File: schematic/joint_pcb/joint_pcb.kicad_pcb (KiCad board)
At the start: 2 copper layers, 0 parts

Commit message: joint pcb power section
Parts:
- added C1: 100u, Capacitor_THT:CP_Radial_D5.0mm_P2.00mm, F.Cu at (64.5, 95.0)
- added C10: 56n, Capacitor_THT:C_Disc_D5.0mm_W2.5mm_P5.00mm, F.Cu at (98.6, 128.9)
- added C11: 5.6n, Capacitor_THT:C_Disc_D5.0mm_W2.5mm_P5.00mm, F.Cu at (106.8, 120.8)
- added C12: 56n, Capacitor_THT:C_Disc_D5.0mm_W2.5mm_P5.00mm, F.Cu at (106.8, 124.9)
- added C13: 100u, Capacitor_THT:CP_Radial_D5.0mm_P2.00mm, F.Cu at (88.9, 94.2)
- added C14: 100nF, Capacitor_THT:C_Disc_D5.0mm_W2.5mm_P5.00mm, F.Cu at (93.8, 137.0)
- added C15: ECE-A1HN101U, Capacitor_THT:CP_Radial_D10.0mm_P5.00mm, F.Cu at (51.8, 73.2)
- added C16: C324C106K3R5TA, Capacitor_THT:C_Disc_D3.8mm_W2.6mm_P2.50mm, F.Cu at (55.9, 60.5)
- added C17: K104Z15Y5VE5TL2, Capacitor_THT:C_Disc_D3.8mm_W2.6mm_P2.50mm, F.Cu at (49.8, 60.5)
- added C18: ECA-1EM100B, Capacitor_THT:CP_Radial_Tantal_D5.0mm_P5.00mm, F.Cu at (81.5, 84.3)
- added C19: ECA-1EM100B, Capacitor_THT:CP_Radial_Tantal_D5.0mm_P5.00mm, F.Cu at (76.5, 52.6)
- added C2: 10u, Capacitor_THT:CP_Radial_D5.0mm_P2.00mm, F.Cu at (79.5, 95.2)
- added C20: EEU-FC1H102L, Capacitor_THT:CP_Radial_D12.5mm_P5.00mm, F.Cu at (111.0, 47.0)
- added C21: C324C106K3R5TA, Capacitor_THT:C_Disc_D3.8mm_W2.6mm_P2.50mm, F.Cu at (136.1, 57.2)
- added C22: K104Z15Y5VE5TL2, Capacitor_THT:C_Disc_D3.8mm_W2.6mm_P2.50mm, F.Cu at (141.2, 57.2)
- added C3: 10u, Capacitor_THT:CP_Radial_D5.0mm_P2.00mm, F.Cu at (72.4, 94.0)
- added C4: 4.7n, Capacitor_THT:C_Disc_D5.0mm_W2.5mm_P5.00mm, F.Cu at (128.3, 126.0)
- added C5: 47n, Capacitor_THT:C_Disc_D5.0mm_W2.5mm_P5.00mm, F.Cu at (98.6, 133.0)
- added C6: 100nF, Capacitor_THT:C_Disc_D5.0mm_W2.5mm_P5.00mm, F.Cu at (98.6, 120.8)
- added C7: 4.7n, Capacitor_THT:C_Disc_D5.0mm_W2.5mm_P5.00mm, F.Cu at (98.6, 124.9)
- added C8: 5.6n, Capacitor_THT:C_Disc_D5.0mm_W2.5mm_P5.00mm, F.Cu at (112.0, 116.8)
- added C9: 100nF, Capacitor_THT:C_Disc_D5.0mm_W2.5mm_P5.00mm, F.Cu at (106.8, 128.9)
- added D1: 1N4148, Diode_THT:D_DO-35_SOD27_P7.62mm_Horizontal, F.Cu at (71.1, 80.8)
- added D2: 1N4148, Diode_THT:D_DO-35_SOD27_P7.62mm_Horizontal, F.Cu at (71.1, 60.5)
- added D3: 1N4148, Diode_THT:D_DO-35_SOD27_P7.62mm_Horizontal, F.Cu at (89.4, 49.5)
- added D4: 1N4148, Diode_THT:D_DO-35_SOD27_P7.62mm_Horizontal, F.Cu at (89.7, 59.7)
- added D5: 1N4148, Diode_THT:D_DO-35_SOD27_P7.62mm_Horizontal, F.Cu at (89.7, 74.9)
- added D6: 1N4148, Diode_THT:D_DO-35_SOD27_P7.62mm_Horizontal, F.Cu at (89.7, 85.1)
- added H1: MountingHole, MountingHole:MountingHole_4.3mm_M4, F.Cu at (139.2, 136.1)
- added H2: MountingHole, MountingHole:MountingHole_4.3mm_M4, F.Cu at (138.7, 48.8)
- added H3: MountingHole, MountingHole:MountingHole_4.3mm_M4, F.Cu at (49.8, 137.2)
- added H4: MountingHole, MountingHole:MountingHole_4.3mm_M4, F.Cu at (49.8, 48.8)
- added IC1: ADA4891-2ARMZ-R7, Package_SO:SOIC-8-1EP_3.9x4.9mm_P1.27mm_EP2.41x3.3mm_ThermalVias, F.Cu at (88.0, 138.2)
- added IC2: LM361N_NOPB, Package_DIP:DIP-14_W7.62mm_Socket_LongPads, F.Cu at (60.8, 124.2)
- added J1: Screw_Terminal_01x04, TerminalBlock_Phoenix:TerminalBlock_Phoenix_PT-1,5-4-3.5-H_1x04_P3.50mm_Horizontal, F.Cu at (51.8, 91.2)
- added J2: Amp_Power, TerminalBlock_Phoenix:TerminalBlock_Phoenix_PT-1,5-2-3.5-H_1x02_P3.50mm_Horizontal, F.Cu at (129.3, 49.0)
- added J3: Audio OUTPUT, TerminalBlock_Phoenix:TerminalBlock_Phoenix_PT-1,5-2-3.5-H_1x02_P3.50mm_Horizontal, F.Cu at (138.7, 72.8)
- added Q1: IRF530A, digikey-footprints:TO-220-3, F.Cu at (111.8, 66.0)
- added Q2: IRF530A, digikey-footprints:TO-220-3, F.Cu at (125.0, 66.0)
- added Q3: IRF530A, digikey-footprints:TO-220-3, F.Cu at (111.8, 76.2)
- added Q4: IRF530A, digikey-footprints:TO-220-3, F.Cu at (125.0, 76.2)
- added R1: 10k, Resistor_THT:R_Axial_DIN0207_L6.3mm_D2.5mm_P10.16mm_Horizontal, F.Cu at (101.4, 104.6)
- added R10: 10k, Resistor_THT:R_Axial_DIN0207_L6.3mm_D2.5mm_P10.16mm_Horizontal, F.Cu at (101.4, 108.7)
- added R11: 8.2k, Resistor_THT:R_Axial_DIN0207_L6.3mm_D2.5mm_P10.16mm_Horizontal, F.Cu at (72.0, 134.5)
- added R12: 1k, Resistor_THT:R_Axial_DIN0207_L6.3mm_D2.5mm_P10.16mm_Horizontal, F.Cu at (85.3, 120.8)
- added R13: 8.2k, Resistor_THT:R_Axial_DIN0207_L6.3mm_D2.5mm_P10.16mm_Horizontal, F.Cu at (114.7, 104.6)
- added R14: 680, Resistor_THT:R_Axial_DIN0207_L6.3mm_D2.5mm_P10.16mm_Horizontal, F.Cu at (85.3, 128.9)
- added R15: 15k, Resistor_THT:R_Axial_DIN0207_L6.3mm_D2.5mm_P10.16mm_Horizontal, F.Cu at (98.6, 116.8)
- added R16: 560, Resistor_THT:R_Axial_DIN0207_L6.3mm_D2.5mm_P10.16mm_Horizontal, F.Cu at (85.3, 133.0)
- added R17: 18k, Resistor_THT:R_Axial_DIN0207_L6.3mm_D2.5mm_P10.16mm_Horizontal, F.Cu at (72.0, 138.6)
- added R18: 10k, Resistor_THT:R_Axial_DIN0207_L6.3mm_D2.5mm_P10.16mm_Horizontal, F.Cu at (85.3, 124.9)
- added R19: 10k, Resistor_THT:R_Axial_DIN0207_L6.3mm_D2.5mm_P10.16mm_Horizontal, F.Cu at (101.4, 112.7)
- added R2: 1k, Resistor_THT:R_Axial_DIN0207_L6.3mm_D2.5mm_P10.16mm_Horizontal, F.Cu at (72.0, 130.5)
- added R20: 10k, Resistor_THT:R_Axial_DIN0207_L6.3mm_D2.5mm_P10.16mm_Horizontal, F.Cu at (88.1, 104.6)
- added R21: CFR-25JB-52-470R, Resistor_THT:R_Axial_DIN0207_L6.3mm_D2.5mm_P10.16mm_Horizontal, F.Cu at (71.1, 75.7)
- added R22: CFR-25JB-52-470R, Resistor_THT:R_Axial_DIN0207_L6.3mm_D2.5mm_P10.16mm_Horizontal, F.Cu at (71.1, 65.5)
- added R23: MFP-25BRD52-1K, Resistor_THT:R_Axial_DIN0207_L6.3mm_D2.5mm_P10.16mm_Horizontal, F.Cu at (71.1, 70.6)
- added R24: CFR-25JR-52-100R, Resistor_THT:R_Axial_DIN0207_L6.3mm_D2.5mm_P10.16mm_Horizontal, F.Cu at (98.6, 54.4)
- added R25: CFR-25JR-52-100R, Resistor_THT:R_Axial_DIN0207_L6.3mm_D2.5mm_P10.16mm_Horizontal, F.Cu at (98.6, 64.5)
- added R26: CFR50SJT-52-10K, Resistor_THT:R_Axial_DIN0207_L6.3mm_D2.5mm_P10.16mm_Horizontal, F.Cu at (119.4, 59.4)
- added R27: CFR50SJT-52-10K, Resistor_THT:R_Axial_DIN0207_L6.3mm_D2.5mm_P10.16mm_Horizontal, F.Cu at (132.6, 59.4)
- added R28: CFR50SJT-52-10K, Resistor_THT:R_Axial_DIN0207_L6.3mm_D2.5mm_P10.16mm_Horizontal, F.Cu at (132.6, 82.8)
- added R29: CFR50SJT-52-10K, Resistor_THT:R_Axial_DIN0207_L6.3mm_D2.5mm_P10.16mm_Horizontal, F.Cu at (119.4, 82.8)
- added R3: 10k, Resistor_THT:R_Axial_DIN0207_L6.3mm_D2.5mm_P10.16mm_Horizontal, F.Cu at (72.0, 126.4)
- added R30: CFR-25JR-52-100R, Resistor_THT:R_Axial_DIN0207_L6.3mm_D2.5mm_P10.16mm_Horizontal, F.Cu at (88.4, 69.6)
- added R31: CFR-25JR-52-100R, Resistor_THT:R_Axial_DIN0207_L6.3mm_D2.5mm_P10.16mm_Horizontal, F.Cu at (88.4, 79.8)
- added R4: 10k, Resistor_THT:R_Axial_DIN0207_L6.3mm_D2.5mm_P10.16mm_Horizontal, F.Cu at (72.0, 122.4)
- added R5: 1.2k, Resistor_THT:R_Axial_DIN0207_L6.3mm_D2.5mm_P10.16mm_Horizontal, F.Cu at (85.3, 116.8)
- added R6: 5.6k, Resistor_THT:R_Axial_DIN0207_L6.3mm_D2.5mm_P10.16mm_Horizontal, F.Cu at (72.0, 118.3)
- added R7: 10k, Resistor_THT:R_Axial_DIN0207_L6.3mm_D2.5mm_P10.16mm_Horizontal, F.Cu at (72.0, 114.3)
- added R8: 1.2k, Resistor_THT:R_Axial_DIN0207_L6.3mm_D2.5mm_P10.16mm_Horizontal, F.Cu at (88.1, 112.7)
- added R9: 10k, Resistor_THT:R_Axial_DIN0207_L6.3mm_D2.5mm_P10.16mm_Horizontal, F.Cu at (88.1, 108.7)
- added U1: LM7805_TO220, Package_TO_SOT_THT:TO-220-3_Vertical, F.Cu at (51.8, 108.5)
- added U2: LM324, Package_DIP:DIP-14_W7.62mm_Socket_LongPads, F.Cu at (60.8, 104.7)
- added U3: HIP4082IP, Package_DIP:DIP-16_W7.62mm, F.Cu at (75.2, 60.5)
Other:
- board outline added: 100 x 100 mm

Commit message: add trace
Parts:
- moved U1 185.7 mm to (237.2, 96.3), turned to 0 degrees
- moved C1 173.7 mm to (237.2, 113.8)
- moved C2 165.3 mm to (244.4, 105.7)
- moved C3 159.2 mm to (229.1, 122.4)
- moved C13 156.0 mm to (243.9, 112.2)
- moved R2 155.4 mm to (222.2, 90.4)
- moved R4 152.7 mm to (222.2, 94.4)
- moved R6 151.5 mm to (222.2, 98.5)
- moved R9 148.6 mm to (235.5, 90.4)
- moved C10 147.8 mm to (243.6, 100.4)
- moved R17 143.8 mm to (208.9, 94.4)
- moved IC1 143.3 mm to (228.0, 107.8)
- moved C5 140.7 mm to (235.5, 100.4)
- moved R11 140.5 mm to (208.9, 102.5)
- moved R7 140.0 mm to (212.0, 114.7)
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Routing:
- net Vcc: track 0.00 -> 92.3 mm
- net +15V: track 0.00 -> 87.7 mm
- net OUT+: track 0.00 -> 83.7 mm
- net OUT-: track 0.00 -> 82.9 mm
- net Net-(D5-Pad2): track 0.00 -> 39.7 mm
- net Net-(D4-Pad2): track 0.00 -> 38.8 mm
- net Net-(D3-Pad2): track 0.00 -> 21.6 mm
- net Net-(D6-Pad2): track 0.00 -> 21.5 mm
- net Net-(C18-Pad2): track 0.00 -> 19.5 mm
- net /Power stage/AHO: track 0.00 -> 17.0 mm
- net Net-(R21-Pad1): track 0.00 -> 14.8 mm
- net /Power stage/ALO: track 0.00 -> 14.8 mm
- net Net-(C19-Pad1): track 0.00 -> 14.0 mm
- net /Power stage/BLO: track 0.00 -> 13.8 mm
- net /Power stage/BHO: track 0.00 -> 13.8 mm
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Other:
- board text added: "+10V"
- board text added: "+15V"
- board text added: "GND"
- board text added: "L"
- board text added: "OUT+"
- board text added: "OUT-"
- board text added: "R"

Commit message: Fixed PCB
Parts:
- C1: value 100u -> 47n; footprint Capacitor_THT:CP_Radial_D5.0mm_P2.00mm -> Capacitor_THT:C_Disc_D5.0mm_W2.5mm_P5.00mm
- C10: value 56n -> 10u; footprint Capacitor_THT:C_Disc_D5.0mm_W2.5mm_P5.00mm -> Capacitor_THT:CP_Radial_D5.0mm_P2.00mm
- C11: value 5.6n -> 10u; footprint Capacitor_THT:C_Disc_D5.0mm_W2.5mm_P5.00mm -> Capacitor_THT:CP_Radial_D5.0mm_P2.00mm
- C12: value 56n -> 100nF
- C13: value 100u -> 100nF; footprint Capacitor_THT:CP_Radial_D5.0mm_P2.00mm -> Capacitor_THT:C_Disc_D5.0mm_W2.5mm_P5.00mm
- C2, C3: value 10u -> 56n; footprint Capacitor_THT:CP_Radial_D5.0mm_P2.00mm -> Capacitor_THT:C_Disc_D5.0mm_W2.5mm_P5.00mm
- C4: value 4.7n -> 100u; footprint Capacitor_THT:C_Disc_D5.0mm_W2.5mm_P5.00mm -> Capacitor_THT:CP_Radial_D5.0mm_P2.00mm
- C5: value 47n -> 4.7n
- C6: value 100nF -> 100u; footprint Capacitor_THT:C_Disc_D5.0mm_W2.5mm_P5.00mm -> Capacitor_THT:CP_Radial_D5.0mm_P2.00mm
- C7: value 4.7n -> 5.6n
- C9: value 100nF -> 4.7n
- IC1: value ADA4891-2ARMZ-R7 -> LM361N_NOPB; footprint Package_SO:SOIC-8-1EP_3.9x4.9mm_P1.27mm_EP2.41x3.3mm_ThermalVias -> Package_DIP:DIP-14_W7.62mm_Socket_LongPads
- IC2: value LM361N_NOPB -> ADA4891-2ARMZ-R7; footprint Package_DIP:DIP-14_W7.62mm_Socket_LongPads -> Package_SO:SOIC-8-1EP_3.9x4.9mm_P1.27mm_EP2.41x3.3mm_ThermalVias
- R11: value 8.2k -> 5.6k
- R12: value 1k -> 10k
- R13: value 8.2k -> 1.2k
- R14: value 680 -> 1k
- R15: value 15k -> 10k
- R16: value 560 -> 8.2k
- R17: value 18k -> 10k
- R2: value 1k -> 1.2k
- R20, R4: value 10k -> 1k
- R3: value 10k -> 8.2k
- R5: value 1.2k -> 10k
- R6: value 5.6k -> 680
- R7: value 10k -> 15k
- R8: value 1.2k -> 560
- R9: value 10k -> 18k
- U1: value LM7805_TO220 -> LM324; footprint Package_TO_SOT_THT:TO-220-3_Vertical -> Package_DIP:DIP-14_W7.62mm_Socket_LongPads
- U2: value LM324 -> LM7805_TO220; footprint Package_DIP:DIP-14_W7.62mm_Socket_LongPads -> Package_TO_SOT_THT:TO-220-3_Vertical
- moved C10 173.1 mm to (70.9, 112.4), turned to 270 degrees
- moved C11 163.3 mm to (70.9, 120.9), turned to 90 degrees
- moved R1 145.1 mm to (66.9, 106.6)
- moved R4 142.5 mm to (80.2, 106.6), turned to 270 degrees
- moved C1 142.4 mm to (94.8, 117.7), turned to 180 degrees
- moved C2 142.1 mm to (103.8, 125.7)
- moved R6 139.3 mm to (84.7, 121.1)
- moved U2 137.0 mm to (62.9, 115.0), turned to 270 degrees
- moved U1 135.0 mm to (102.4, 104.0)
- moved C5 133.6 mm to (103.7, 122.5)
- moved C4 133.4 mm to (80.3, 101.9), turned to 180 degrees
- moved R2 133.1 mm to (89.3, 97.5)
- moved R18 128.9 mm to (90.3, 141.1), turned to 90 degrees
- moved R17 128.0 mm to (86.2, 131.0), turned to 270 degrees
- moved R9 123.5 mm to (113.8, 111.3)
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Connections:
- C1 pad 2: Input -> Net-(C1-Pad2)
- C10 pad 1: Net-(C10-Pad1) -> Vcc
- C10 pad 2: Net-(C10-Pad2) -> GND
- C11 pad 1: GND -> +5V
- C11 pad 2: Net-(C11-Pad2) -> GND
- C12 pad 1: Net-(C12-Pad1) -> Vcc
- C12 pad 2: Net-(C12-Pad2) -> GND
- C13 pad 1: Net-(C12-Pad1) -> +5V
- C13 pad 2: Net-(C13-Pad2) -> GND
- C14 pad 1: Vcc -> +5V
- C15 pad 1: Vcc -> +10V
- C16 pad 1: Vcc -> +10V
- C17 pad 1: Vcc -> +10V
- C2 pad 1: Vcc -> Net-(C2-Pad1)
- C2 pad 2: GND -> Net-(C2-Pad2)
- C20 pad 1: +15V -> Vcc
- C21 pad 1: +15V -> Vcc
- C22 pad 1: +15V -> Vcc
- C3 pad 1: +5V -> Net-(C3-Pad1)
- C3 pad 2: GND -> Net-(C3-Pad2)
- C4 pad 2: GND -> Input
- C5 pad 2: Net-(C5-Pad2) -> GND
- C6 pad 1: +5V -> Net-(C3-Pad1)
- C6 pad 2: GND -> Net-(C6-Pad2)
- C7 pad 1: Net-(C7-Pad1) -> GND
- C9 pad 1: +5V -> Net-(C9-Pad1)
- C9 pad 2: GND -> Net-(C9-Pad2)
- D1 pad 2: Vcc -> +10V
- D2 pad 2: Vcc -> +10V
- IC1 pad 1: Net-(IC1-Pad1) -> +5V
- IC1 pad 2: Vref -> Net-(IC1-Pad2)
- IC1 pad 3: Net-(IC1-Pad3) -> filterOut
- IC1 pad 4: GND -> Net-(C9-Pad1)
- IC1 pad 5: Vref -> Net-(IC1-Pad5)
- IC1 pad 6: Net-(C7-Pad2) -> GND
- IC1 pad 7: Net-(C7-Pad1) -> Net-(IC1-Pad7)
- IC1 pad 8: +5V -> GND
- IC1 pad 9: (no net) -> PWM-
- IC2 pad 1: +5V -> Net-(IC2-Pad1)
- IC2 pad 2: Net-(IC2-Pad2) -> Vref
- IC2 pad 3: filterOut -> Net-(IC2-Pad3)
- IC2 pad 4: Net-(C7-Pad1) -> GND
- IC2 pad 5: Net-(IC2-Pad5) -> Vref
- IC2 pad 6: GND -> Net-(C9-Pad2)
- IC2 pad 7: Net-(IC2-Pad7) -> Net-(C9-Pad1)
- IC2 pad 8: GND -> +5V
- IC2 pad 9: /Power stage/PWM- -> (no net)
- J2 pad 1: +15V -> Vcc
- Q1 pad 2: +15V -> Vcc
- Q3 pad 2: +15V -> Vcc
- R1 pad 2: Bias -> Net-(C4-Pad1)
- R10 pad 1: Vref -> Net-(C6-Pad2)
- R10 pad 2: GND -> filterOut
- R11 pad 1: Net-(C4-Pad1) -> Net-(R11-Pad1)
- R11 pad 2: Net-(C5-Pad2) -> Net-(R11-Pad2)
- R12 pad 1: Net-(C7-Pad2) -> filterOut
- R12 pad 2: Net-(IC1-Pad1) -> GND
- R13 pad 1: Net-(C7-Pad1) -> Bias
- R13 pad 2: Net-(IC1-Pad3) -> Net-(R11-Pad2)
- R14 pad 1: Net-(C10-Pad1) -> Net-(C9-Pad2)
- R14 pad 2: Net-(C5-Pad1) -> Net-(IC2-Pad1)
- R15 pad 1: Net-(C8-Pad2) -> Net-(IC2-Pad3)
- R15 pad 2: Net-(C10-Pad1) -> Net-(IC2-Pad1)
- R16 pad 1: Net-(C12-Pad2) -> Net-(C9-Pad1)
- R16 pad 2: Net-(C10-Pad2) -> Net-(IC2-Pad3)
- R17 pad 1: Net-(C11-Pad2) -> +5V
- R17 pad 2: Net-(C12-Pad2) -> Vref
- R18 pad 1: Net-(C13-Pad2) -> Vref
- R18 pad 2: filterOut -> GND
- R19 pad 1: +5V -> Vcc
- R19 pad 2: filterOut -> Bias
- R2 pad 1: Bias -> Net-(C1-Pad2)
- R2 pad 2: GND -> Net-(R11-Pad1)
- R20 pad 1: filterOut -> Bias
- R21 pad 2: /Power stage/PWM+ -> PWM+
- R22 pad 2: /Power stage/PWM- -> PWM-
- R3 pad 1: Vcc -> Net-(C5-Pad1)
- R3 pad 2: Net-(C1-Pad1) -> Net-(C1-Pad2)
- R4 pad 1: Net-(C1-Pad1) -> Net-(C4-Pad1)
- R5 pad 1: Bias -> +5V
- R5 pad 2: Net-(R5-Pad2) -> filterOut
- R6 pad 1: Net-(R6-Pad1) -> Net-(C2-Pad1)
- R6 pad 2: Net-(R5-Pad2) -> Net-(C1-Pad1)
- R7 pad 1: Net-(IC1-Pad3) -> Net-(C7-Pad2)
- R7 pad 2: Net-(IC1-Pad1) -> Net-(C2-Pad1)
- R8 pad 1: Net-(C5-Pad2) -> Net-(C3-Pad2)
- R8 pad 2: Net-(R6-Pad1) -> Net-(C2-Pad2)
- R9 pad 1: +5V -> Net-(C8-Pad2)
- R9 pad 2: Vref -> Net-(C3-Pad2)
- U1 pad 1: Vcc -> Net-(R11-Pad1)
- U1 pad 2: GND -> Net-(R11-Pad2)
- U1 pad 3: +5V -> Net-(C4-Pad1)
- U2 pad 1: Net-(R6-Pad1) -> Vcc
- U2 pad 2: Net-(R5-Pad2) -> GND
- U2 pad 3: Net-(C1-Pad1) -> +5V
- U3 pad 12: Vcc -> +10V
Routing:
- net PWM+: track 0.00 -> 145.3 mm
- net PWM-: track 0.00 -> 134.9 mm
- net Vcc: track 92.3 -> 211.6 mm
- net +5V: track 0.00 -> 108.0 mm
- net +15V: track 87.7 -> 0.00 mm
- net +10V: track 0.00 -> 74.1 mm
- net Vref: track 0.00 -> 41.1 mm
- net filterOut: track 0.00 -> 35.6 mm
- net Net-(C4-Pad1): track 0.00 -> 31.1 mm
- net Net-(C3-Pad1): track 0.00 -> 30.7 mm
- net Net-(C9-Pad1): track 0.00 -> 29.5 mm
- net Net-(IC2-Pad1): track 0.00 -> 27.7 mm
- net Bias: track 0.00 -> 26.4 mm
- net Net-(R11-Pad1): track 0.00 -> 25.6 mm
- net Net-(C2-Pad1): track 0.00 -> 23.8 mm
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- added copper zone on B.Cu, net GND
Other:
- board text added: "ADA4891"
- board text added: "LM324"
- board text added: "LM361"

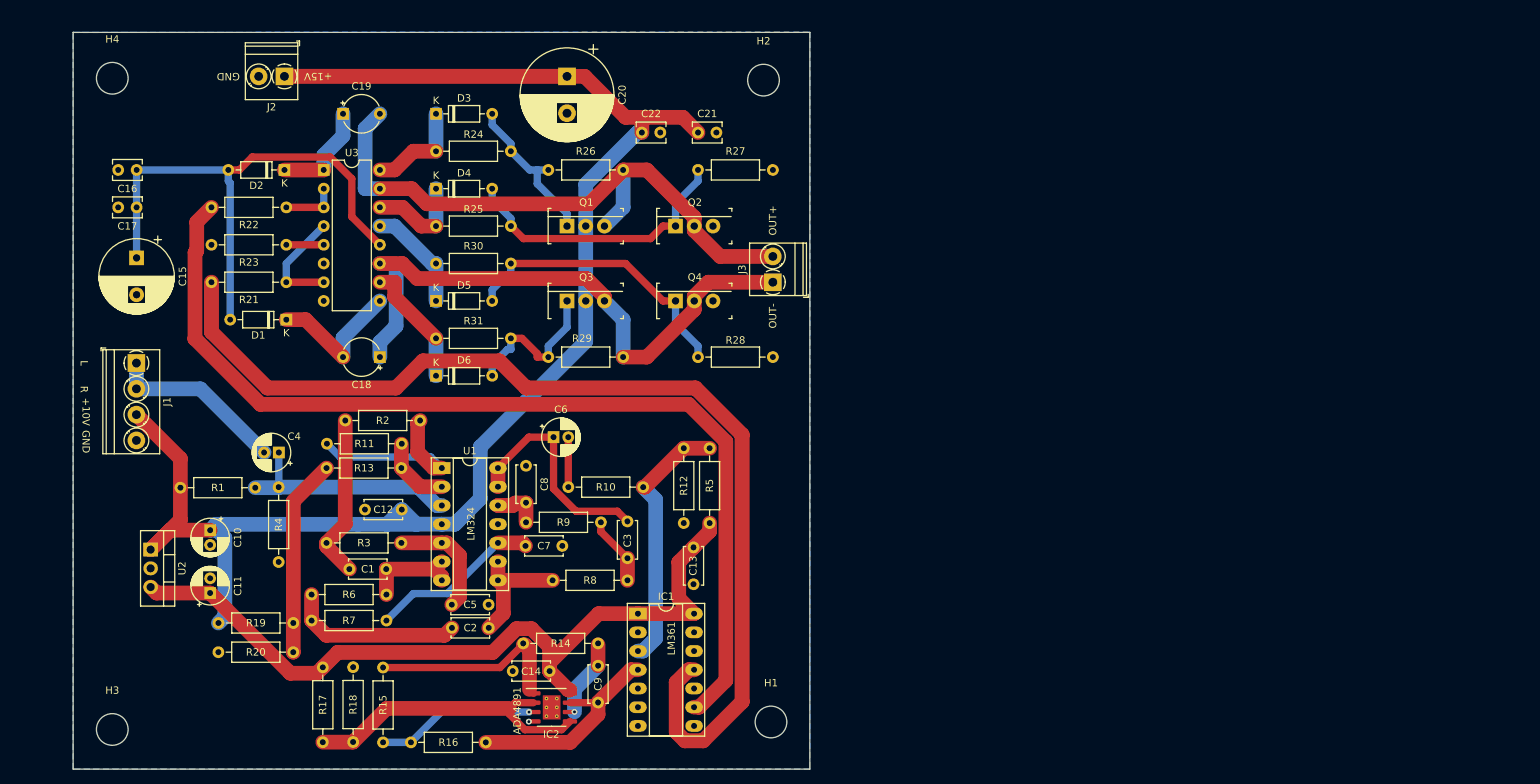
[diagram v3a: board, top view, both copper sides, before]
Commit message: Added ground ouput, aligned mounting holes, rounded corners
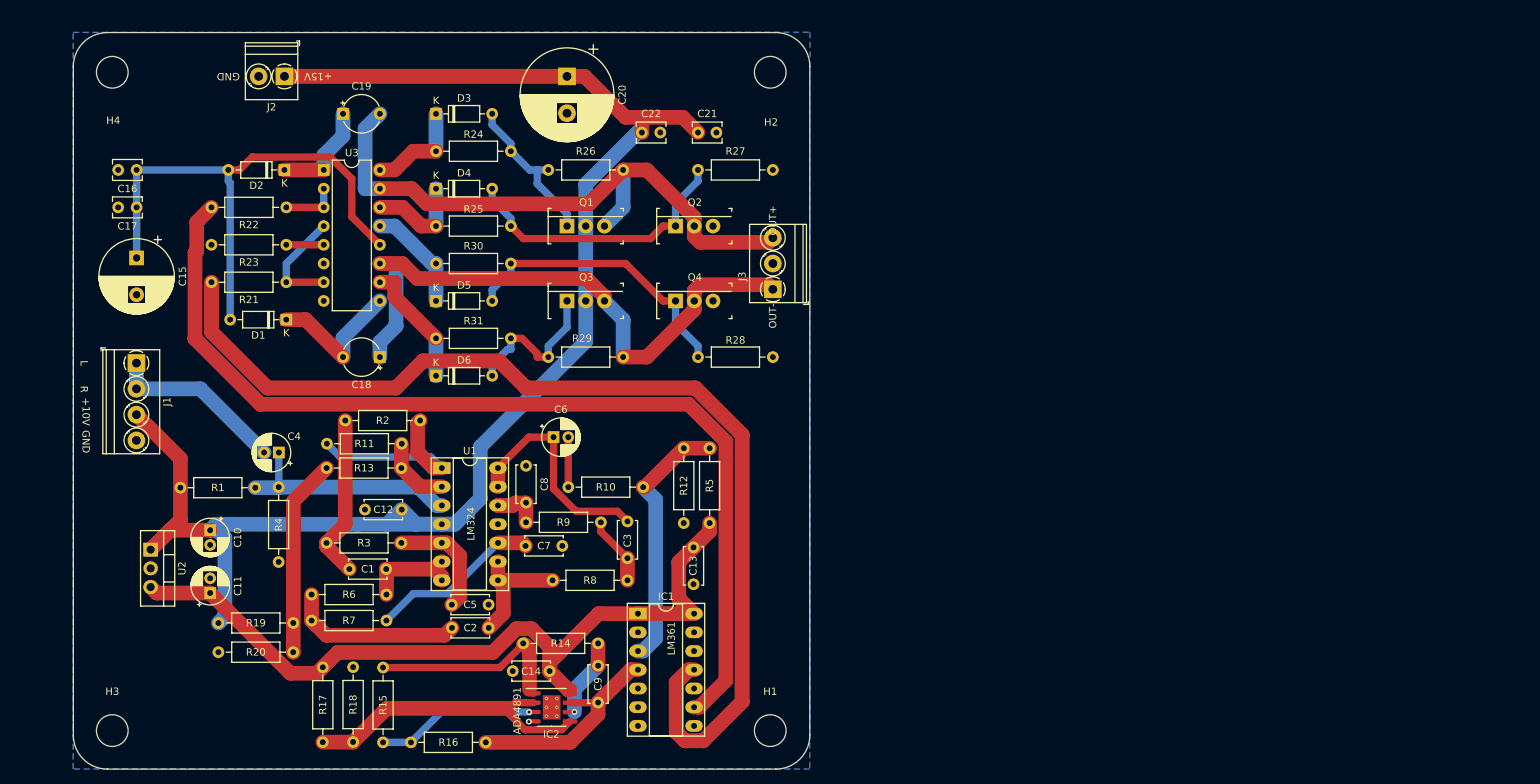
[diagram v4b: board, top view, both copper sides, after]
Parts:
- J3: footprint TerminalBlock_Phoenix:TerminalBlock_Phoenix_PT-1,5-2-3.5-H_1x02_P3.50mm_Horizontal -> TerminalBlock_Phoenix:TerminalBlock_Phoenix_PT-1,5-3-3.5-H_1x03_P3.50mm_Horizontal
- moved H2 1.41 mm to (147.0, 50.2)
- moved H1 1.17 mm to (147.0, 139.6)
- moved J3 0.96 mm to (147.3, 79.7)
- moved H4 0.81 mm to (57.7, 50.2)
- moved H3 0.15 mm to (57.7, 139.6)
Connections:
- J3 pad 2: OUT+ -> GND
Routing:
- net OUT-: track 82.9 -> 83.5 mm
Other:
- outline, holes or cut-outs redrawn
